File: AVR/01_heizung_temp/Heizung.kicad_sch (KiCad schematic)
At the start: 15 parts, among them J1 Analog, J2 Digital, J3 Screw_Terminal_01x03, U1 PC817, U2 TL431LP, U3 DS18B20

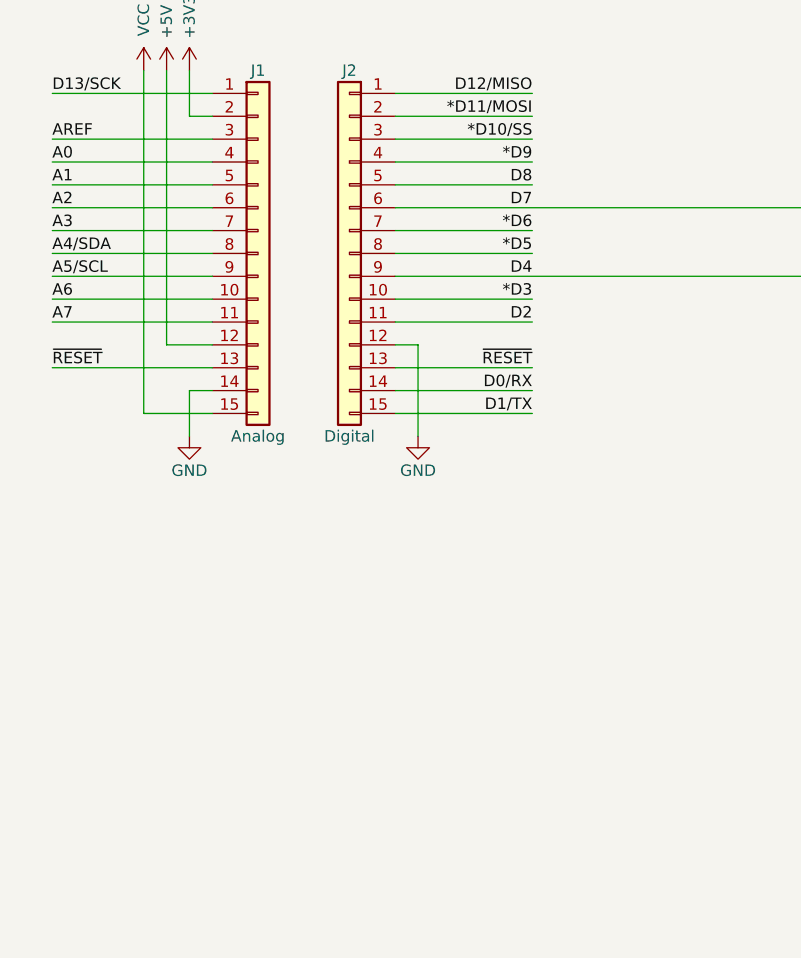
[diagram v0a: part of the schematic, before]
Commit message: report the PWM source; reject the dead-man timeout
The dead-man timeout recommended in doc/risk_analysis.md was wrong, and this
withdraws it.

The error was treating the duty as a lease. A lease expires because it was
granted on information that may since have changed; "hold the house at 55%" is
not that -- it stays true until someone says otherwise. Expiring it would:

- drop the heat on every controller *reboot*, which is far more common than a
  controller dying while still demanding heat, and is precisely when the duty
  is most needed;
- turn a harmless restart into a frozen house, reintroducing the failure the
  EEPROM persistence exists to prevent;
- and it could not distinguish "died while demanding heat" from "died having
  stopped", so it would discard the correct value as often as the wrong one.

A duty can outlive its author. That is right for a setpoint and wrong only if
the controller was acting on information that has since changed -- which is the
controller's problem when it returns, not this node's to guess at by inventing
a safe value.

Replaced by making the source visible rather than bounding the value. PWM_SRC_*
rides in bits 1..2 of the PWM frame's flags byte, on CAN 0x280 and radio 0xABCF
at once, so the two wires cannot disagree:

  EEPROM  restored from the log, nothing is commanding this node
  CAN     last valid command was CAN 0x240
  NRF     last valid command was radio 0xABD0
  FAULT   local safety action, i.e. the PWM ISR stall fallback

A node sitting on EEPROM forever is legible as such, which is the diagnostic a
timeout was being asked to provide -- without the behaviour change that made it
unacceptable.

set_pwm_duty() keeps the current source, so the 1 h duty-change refresh does not
launder EEPROM into being the author of a duty it merely persisted. The four
authoring paths pass their own source explicitly.

Decoders added to AVR/02_nrf_receiver (which annotates the idle summary when
nothing is commanding) and ESP32/26_CYD_CAN_mon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
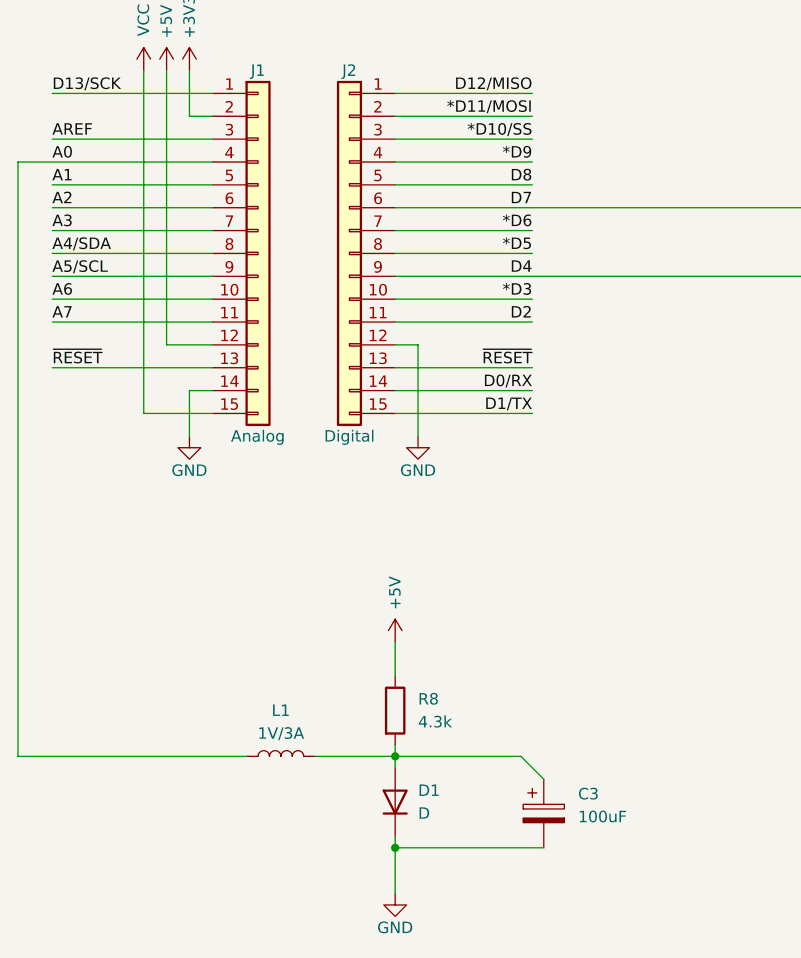
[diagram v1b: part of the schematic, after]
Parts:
- added C3: 100uF, symbol Device:C_Polarized
- added D1: D, symbol Device:D
- added L1: 1V/3A, symbol Device:L
- added R8: 4.3k, symbol Device:R
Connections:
- net +5V: now also R8.1
- net A0: now also L1.1
- net GND: now also C3.2, D1.1 (K)
- new net: C3.1, D1.2 (A), L1.2, R8.2
